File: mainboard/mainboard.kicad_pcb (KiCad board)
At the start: 2 copper layers, 250 x 100 mm, 85 parts, among them K1 G6S-2F-5DC, X1 POWER, X2 IO, X3 INPUT, X4 FRONT INPUT, X5 MAIN OUTPUT, X6 PHONES OUTPUT, X7 UART

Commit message: Fixed selector PCB, relays on different ULN2003 lines, mainboard pcb
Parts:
- moved C29 2.13 mm to (492.8, 234.0), turned to 0 degrees
- moved R4 1.01 mm to (391.8, 208.3)
- moved R19 0.19 mm to (527.8, 218.0)
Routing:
- net GND: track 194.0 -> 221.1 mm, vias 28 -> 18
- net /ROUT: track 69.5 -> 78.8 mm
- net AGND: track 18.1 -> 23.7 mm
- net +3V3: track 390.1 -> 393.7 mm
- net /LOUT: track 61.3 -> 64.5 mm
- net /RE_BTN: track 214.6 -> 211.6 mm
- net /B_MINUS: track 107.2 -> 105.7 mm
- net /PH_SW: track 141.8 -> 143.2 mm
- net /SDA: track 237.1 -> 238.5 mm
- net /B_MUTE: track 54.8 -> 53.5 mm
- net /BOUT_L: track 6.13 -> 4.86 mm
- net Net-(C18-Pad1): track 10.2 -> 8.92 mm
- net /B_SETTINGS: track 61.2 -> 62.0 mm
- net /B_PLUS: track 94.9 -> 95.7 mm
- net Net-(C11-Pad1): track 9.79 -> 9.03 mm
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
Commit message: Simpler mainboard
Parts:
- removed BR1: ALPS-EC11E, utils:RotaryEncoder_Alps_EC11E-Switch_Vertical_H20mm
- removed D1: 3.12'' 256x64 SSD1322 module, WAMP:OLED_SSD1322_256X64_312_MODULE
- removed SB1: DISPLAY, WAMP:BUTTONS_DTS-6
- removed SB2: MUTE, WAMP:BUTTONS_DTS-6
- removed SB3: INPUT, WAMP:BUTTONS_DTS-6
- removed SB4: PHONES, WAMP:BUTTONS_DTS-6
- removed SB5: DEFEAT, WAMP:BUTTONS_DTS-6
- removed SB6: SETTINGS, WAMP:BUTTONS_DTS-6
- removed SB7: PLUS, WAMP:BUTTONS_DTS-6
- removed SB8: MINUS, WAMP:BUTTONS_DTS-6
- added X10: BUTTONS, WAMP:CON_CONN_BL_09X01, F.Cu at (530.5, 235.7)
- added X8: DISPLAY, WAMP:CON_CONN_BL_07X01, F.Cu at (549.3, 194.3)
- added X9: ENCODER, WAMP:CON_CONN_BL_04X01, F.Cu at (549.3, 170.2)
- DA2: value L7809D2T-TR -> L7809V; footprint WAMP:TO508P1016X864X464-2N -> Package_TO_SOT_THT:TO-220-3_Vertical
- moved C22 193.4 mm to (545.5, 173.0), turned to 0 degrees
- moved C12 119.1 mm to (501.9, 233.1), turned to 270 degrees
- moved R4 117.2 mm to (507.4, 227.8), turned to 0 degrees
- moved C14 116.9 mm to (494.9, 235.0), turned to 90 degrees
- moved C11 113.7 mm to (501.9, 228.6), turned to 270 degrees
- moved C13 111.8 mm to (485.4, 235.0), turned to 270 degrees
- moved C10 108.4 mm to (501.9, 224.2), turned to 270 degrees
- moved C21 106.3 mm to (478.4, 233.1), turned to 90 degrees
- moved R5 104.3 mm to (472.7, 234.9)
- moved C17 103.3 mm to (501.9, 219.7), turned to 270 degrees
- moved C20 100.2 mm to (478.4, 228.6), turned to 90 degrees
- moved R12 98.6 mm to (472.7, 228.6), turned to 90 degrees
- moved C5 97.8 mm to (502.2, 214.7), turned to 90 degrees
- moved DA3 97.8 mm to (490.2, 222.3), turned to 0 degrees
- moved C3 97.2 mm to (458.7, 234.3), turned to 90 degrees
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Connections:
- DA2 pad 1: +9V -> +12V
- DA2 pad 2: +12V -> GND
- DA2 pad 3: GND -> +9V
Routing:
- net /RE_B: track 260.8 -> 11.0 mm, vias 1 -> 0
- net /RE_A: track 264.0 -> 14.3 mm, vias 1 -> 2
- net /RE_BTN: track 211.6 -> 33.4 mm, vias 1 -> 2
- net +3V3: track 393.7 -> 222.7 mm, vias 3 -> 7
- net /SDA: track 238.5 -> 110.6 mm, vias 2 -> 5
- net /SCL: track 244.2 -> 117.3 mm, vias 3 -> 8
- net /ADC6: track 150.6 -> 24.6 mm, vias 2 -> 0
- net /ADC7: track 139.5 -> 14.1 mm, vias 2 -> 0
- net GND: track 221.1 -> 125.1 mm, vias 18 -> 14
- net /PH_SW: track 143.2 -> 48.3 mm, vias 0 -> 2
- net /CS0: track 83.0 -> 9.49 mm, vias 0 -> 1
- net /MOSI: track 88.2 -> 16.9 mm, vias 1 -> 0
- net /SCLK: track 87.5 -> 21.8 mm, vias 1 -> 2
- net /B_MINUS: track 105.7 -> 41.4 mm, vias 1 -> 2
- net /B_PLUS: track 95.7 -> 41.1 mm, vias 0 -> 4
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- added copper zone on F.Cu, net +3V3
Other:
- board size 250 x 100 mm -> 110 x 90 mm

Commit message: mainboard pdf
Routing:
- net GND: track 125.1 -> 122.2 mm
- net /SCL: track 117.3 -> 117.9 mm
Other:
- board text added: "WAMP-FA v1.2"

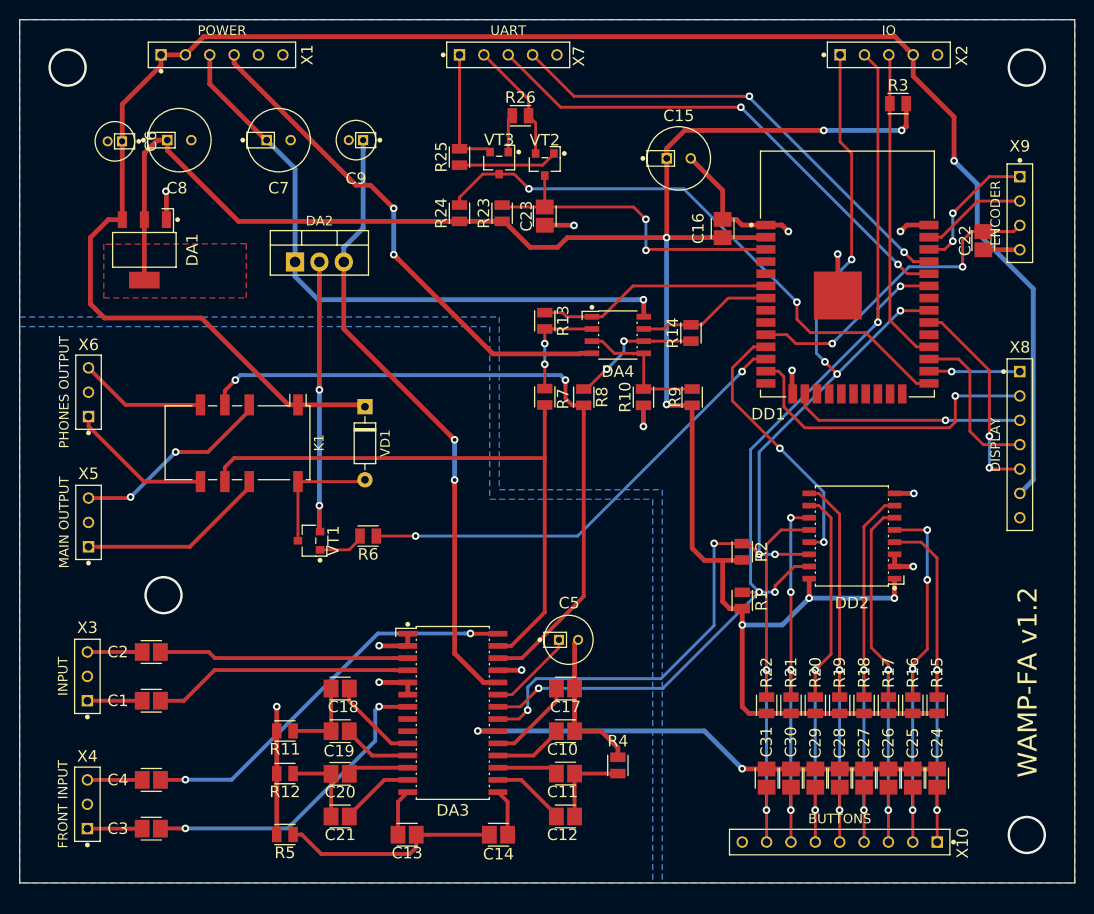
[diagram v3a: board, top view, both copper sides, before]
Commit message: Film caps on MB, new powering scheme, opamp replaced
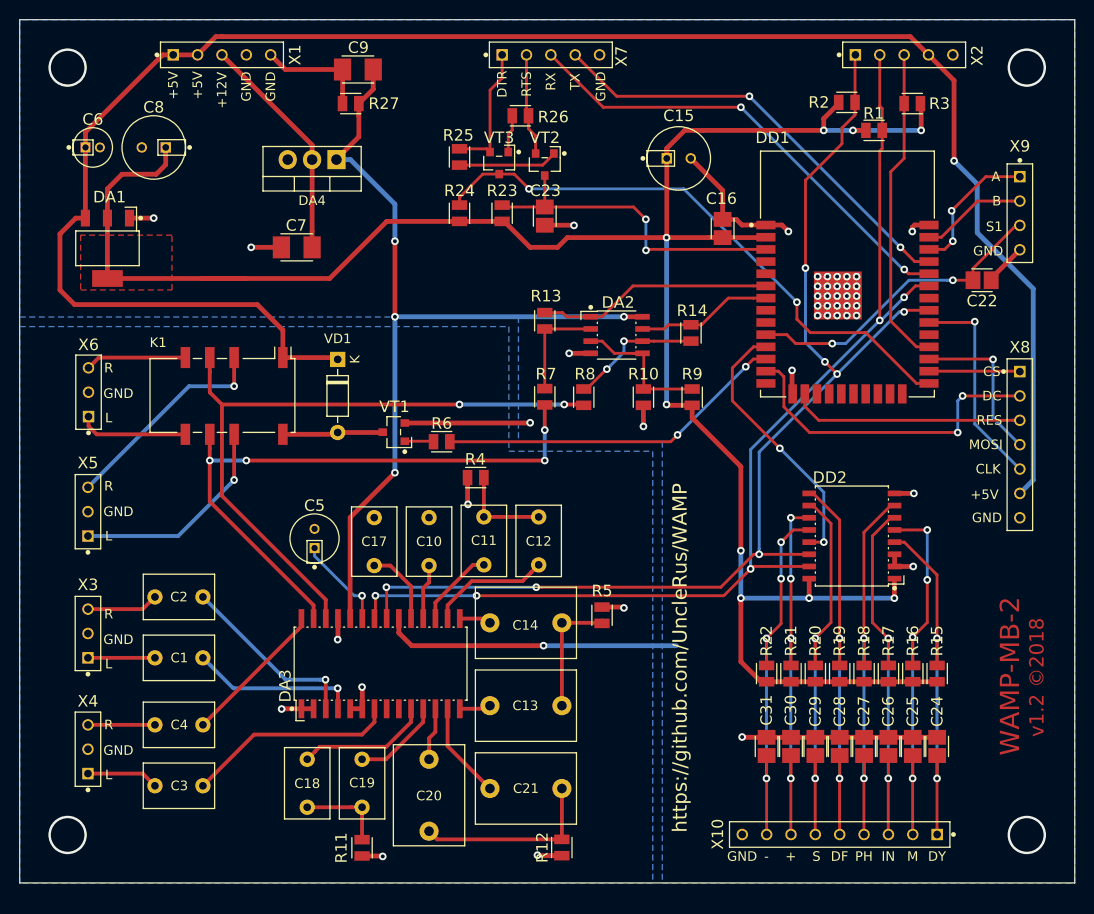
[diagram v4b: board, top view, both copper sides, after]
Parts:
- added R27: 3k3, WAMP:RESC2013X65N, F.Cu at (479.5, 158.8)
- C1, C11, C12, C18, C19, C2, C3, C4: footprint WAMP:CAPC2013X140N -> Capacitor_THT:C_Rect_L7.2mm_W4.5mm_P5.00mm_FKS2_FKP2_MKS2_MKP2
- C10, C17: footprint WAMP:CAPC2013X140N -> Capacitor_THT:C_Rect_L7.0mm_W4.5mm_P5.00mm
- C13, C14, C20, C21: footprint WAMP:CAPC2013X140N -> Capacitor_THT:C_Rect_L10.3mm_W7.2mm_P7.50mm_MKS4
- C7: value 100uF -> 330n; footprint WAMP:CAPPRD250W50D650H1300N -> WAMP:CAPC3216X180N
- C9: value 10uF -> 100n; footprint WAMP:CAPPRD150W45D400H800N -> WAMP:CAPC3216X180N
- DA2: value L7809V -> LM358DT; footprint Package_TO_SOT_THT:TO-220-3_Vertical -> WAMP:SOIC127P600X175-8N
- DA4: value TL072CD -> L7809; footprint WAMP:SOIC127P600X175-8N -> Package_TO_SOT_THT:TO-220-3_Vertical
- X1: footprint WAMP:CON_CONN_BL_06X01 -> WAMP:CON_CONN_BL_05X01
- moved R1 50.9 mm to (534.1, 161.5), turned to 90 degrees
- moved R2 48.1 mm to (531.2, 158.6), turned to 90 degrees
- moved R5 40.2 mm to (505.7, 212.1), turned to 0 degrees
- moved DA4 34.6 mm to (478.0, 164.6), turned to 180 degrees
- moved DA2 34.4 mm to (507.2, 182.9)
- moved R4 33.5 mm to (492.5, 197.7), turned to 90 degrees
- moved C12 31.4 mm to (499.1, 201.8)
- moved R12 29.9 mm to (501.5, 236.3), turned to 180 degrees
- moved C5 28.5 mm to (475.7, 204.1), turned to 180 degrees
- moved C11 28.1 mm to (493.4, 201.8)
- moved C17 26.7 mm to (482.0, 201.9)
- moved C10 26.4 mm to (487.7, 201.9)
- moved C21 23.3 mm to (501.5, 230.2), turned to 180 degrees
- moved C14 23.1 mm to (501.5, 212.9), turned to 180 degrees
- moved C13 21.0 mm to (501.5, 221.5), turned to 180 degrees
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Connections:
- C7 pad 1: +12V -> Net-(C7-Pad1)
- DA2 pad 1: +12V -> /ADC6
- DA2 pad 2: GND -> Net-(DA2-Pad2)
- DA2 pad 3: +9V -> Net-(DA2-Pad3)
- DA4 pad 1: /ADC6 -> +9V
- DA4 pad 2: Net-(DA4-Pad2) -> Net-(C7-Pad1)
- DA4 pad 3: Net-(DA4-Pad3) -> GND
- R10 pad 1: Net-(DA4-Pad3) -> Net-(DA2-Pad3)
- R13 pad 1: Net-(DA4-Pad2) -> Net-(DA2-Pad2)
- R14 pad 2: Net-(DA4-Pad6) -> Net-(DA2-Pad6)
- R7 pad 2: Net-(DA4-Pad2) -> Net-(DA2-Pad2)
- R8 pad 2: Net-(DA4-Pad6) -> Net-(DA2-Pad6)
- R9 pad 2: Net-(DA4-Pad3) -> Net-(DA2-Pad3)
- X1 pad 3: +12V -> Net-(C7-Pad1)
- X1 pad 4: -12V -> GND
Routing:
- net +12V: track 66.0 -> 0.00 mm, vias 1 -> 0
- net -12V: track 53.6 -> 0.00 mm, vias 2 -> 0
- net Net-(C4-Pad2): track 41.5 -> 15.3 mm, vias 2 -> 0
- net +9V: track 64.9 -> 90.0 mm, vias 2 -> 4
- net Net-(C7-Pad1): track 0.00 -> 24.0 mm
- net AGND: track 40.3 -> 19.0 mm, vias 4 -> 7
- net Net-(DA4-Pad3): track 14.7 -> 0.00 mm
- net Net-(DA2-Pad3): track 0.00 -> 14.7 mm
- net Net-(DA4-Pad6): track 13.9 -> 0.00 mm, vias 2 -> 0
- net Net-(DA2-Pad6): track 0.00 -> 13.9 mm, vias 0 -> 2
- net /PH_SW: track 48.3 -> 36.5 mm
- net Net-(DA4-Pad2): track 11.1 -> 0.00 mm, vias 2 -> 0
- net Net-(DA2-Pad2): track 0.00 -> 11.1 mm
- net Net-(C20-Pad1): track 8.42 -> 19.5 mm
- net Net-(C3-Pad2): track 32.9 -> 22.0 mm, vias 2 -> 0
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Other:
- board text added: "+"
- board text added: "+12V"
- board text added: "+5V"
- board text added: "-"
- board text added: "A"
- board text added: "B"
- board text added: "CLK"
- board text added: "CS"
- board text added: "DC"
- board text added: "DF"
- board text added: "DTR"
- board text added: "DY"
- board text added: "GND"
- board text added: "IN"
- board text added: "L"
- board text added: "M"
- board text added: "MOSI"
- board text added: "PH"
- board text added: "R"
- board text added: "RES"
- board text added: "RTS"
- board text added: "RX"
- board text added: "S"
- board text added: "S1"
- board text added: "TX"
- board text added: "WAMP-MB-2"
- board text added: "https://github.com/UncleRus/WAMP"
- board text added: "v1.2 ©2018"
- board text removed: "WAMP-FA v1.2"
